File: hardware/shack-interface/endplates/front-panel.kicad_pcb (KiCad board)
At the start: 2 copper layers, 165 x 51.1 mm, 4 parts

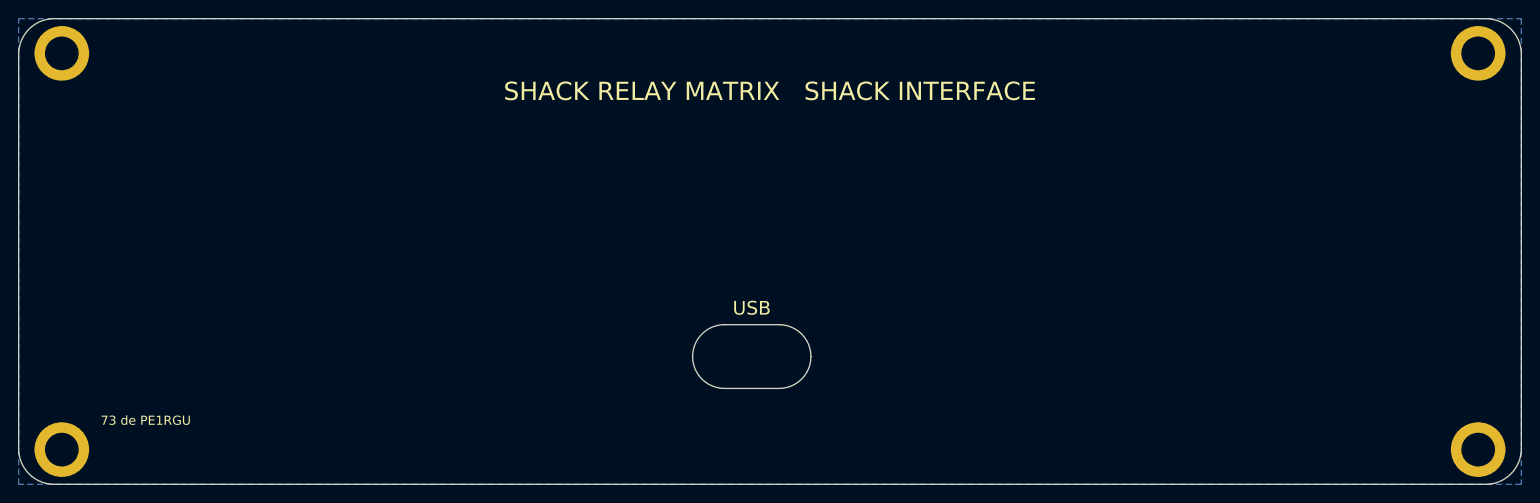
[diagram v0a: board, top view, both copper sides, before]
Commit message: Shack interface: end plates, schematic and PCB update; design log
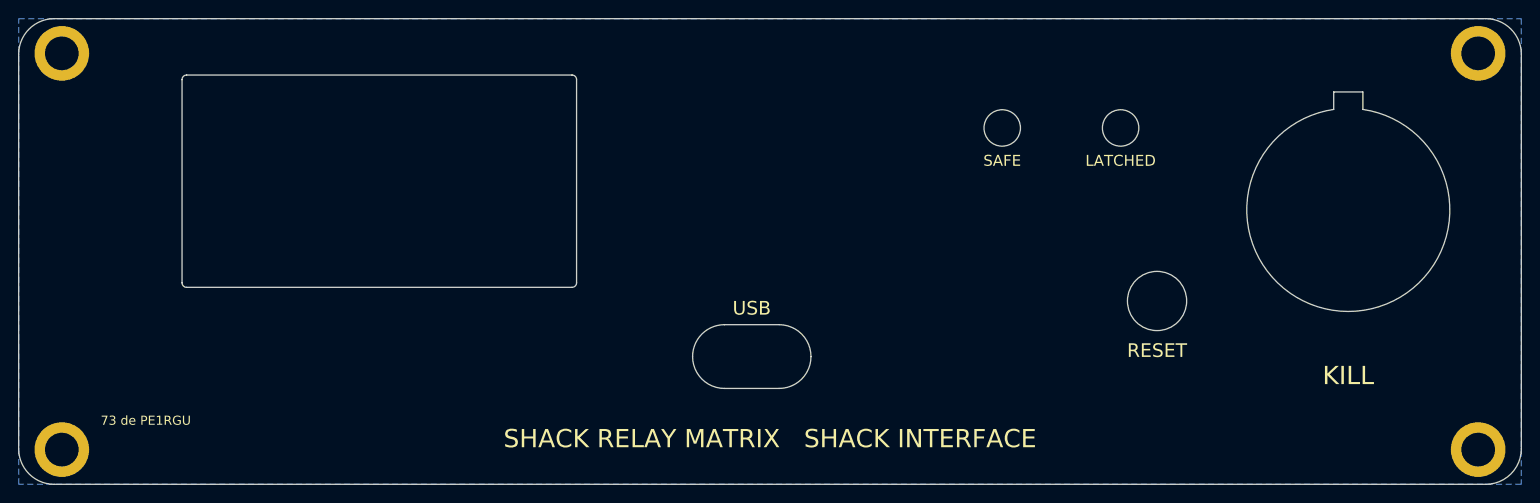
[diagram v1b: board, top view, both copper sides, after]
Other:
- outline, holes or cut-outs redrawn
- board text added: "KILL"
- board text added: "LATCHED"
- board text added: "RESET"
- board text added: "SAFE"
- board text added: "SRM shack interface front plate rev A (a3) 2026-10"
- board text removed: "SRM shack interface front plate rev A (a1) 2026-10"
